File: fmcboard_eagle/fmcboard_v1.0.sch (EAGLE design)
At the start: 63 parts, among them IC1 OPA699ID, IC2 OPA699ID, IC3 ICL7660CPA, IC4 ICL7660CPA, IC5 LM358, J1 8pin, J12 4p-2.54, J2 ASP-134604-01, J3 4p-2.54, J4 4p-2.54, J5 8pin, J6 4p-2.54, Q1 BSS138, Q2 BSS138, Q3 BSS138, Q4 BSS138

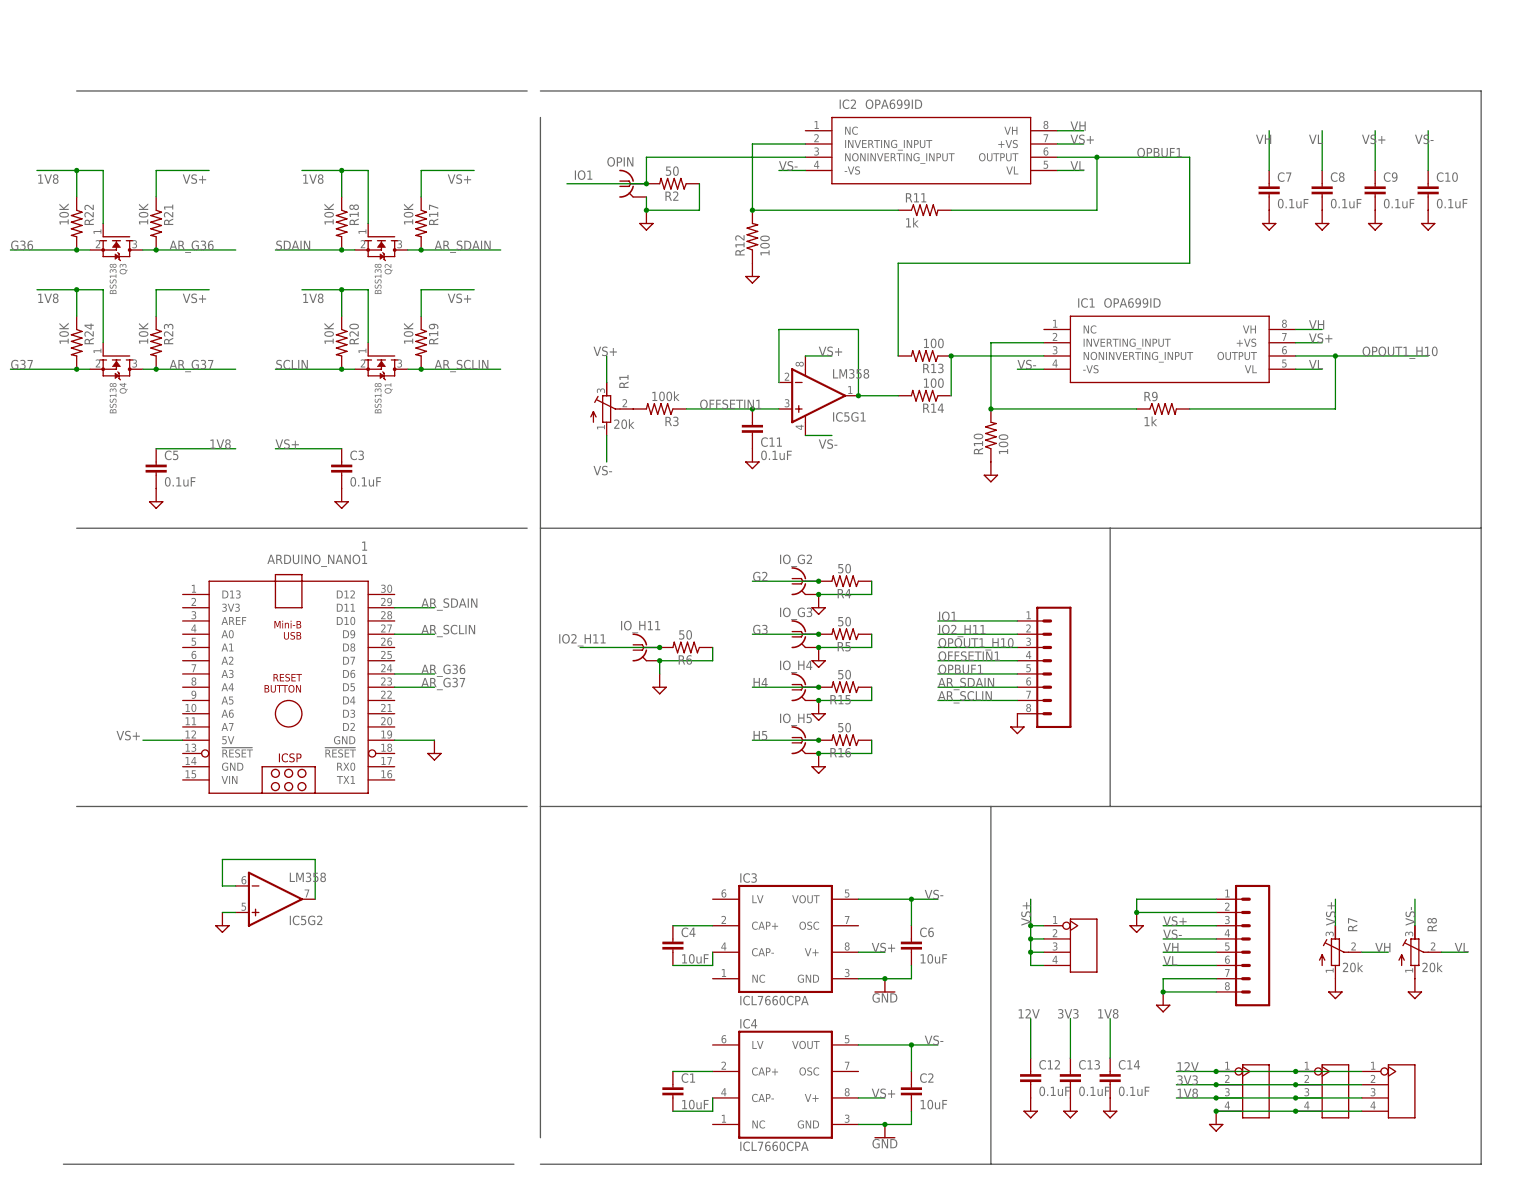
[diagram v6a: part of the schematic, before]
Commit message: Revert "use bss138 level shifting"
This reverts commit dd6467e355429a32c42db6855984b6cad7435a14.
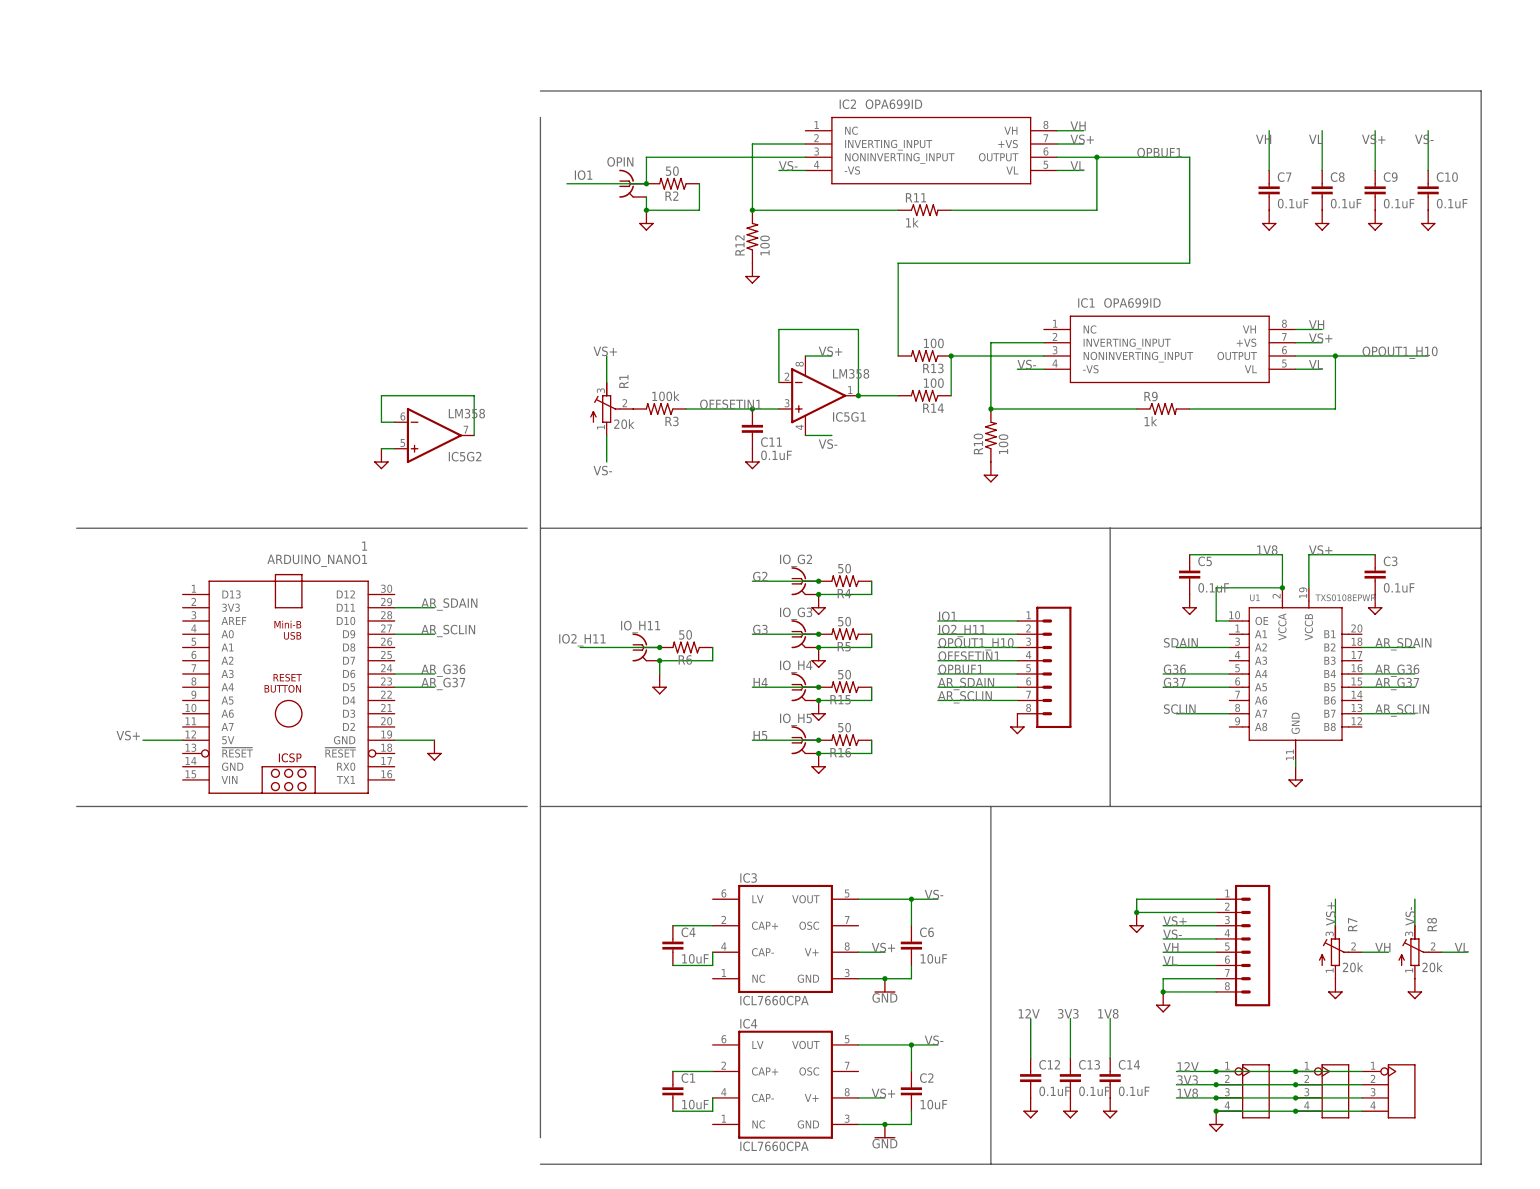
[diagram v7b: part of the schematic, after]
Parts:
- removed J6: 4p-2.54, Seeed-Connector:DIP-BLACK-FEMALE-HEADER-VERT(4P-2.54)
- removed Q1, Q2, Q3, Q4: BSS138, adafruit:MOSFET-NREFLOW
- removed R17, R18, R19, R20, R21, R22, R23, R24: 10K, adafruit:R-US_R0805
- added U1: TXS0108EPWR, Seeed-IC:LOGIC-TXS0108EPWR(TSSOP20)
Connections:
- net 1V8: now also U1.OE, U1.VCCA; no longer Q1.G, Q2.G, Q3.G, Q4.G, R18.1, R20.1, R22.1, R24.1
- net AR_G36: now also U1.B4; no longer Q3.D, R21.2
- net AR_G37: now also U1.B5; no longer Q4.D, R23.2
- net AR_SCLIN: now also U1.B7; no longer Q1.D, R19.2
- net AR_SDAIN: now also U1.B2; no longer Q2.D, R17.2
- net G36: now also U1.A4; no longer Q3.S, R22.2
- net G37: now also U1.A5; no longer Q4.S, R24.2
- net GND: now also U1.GND
- net SCLIN: now also U1.A7; no longer Q1.S, R20.2
- net SDAIN: now also U1.A2; no longer Q2.S, R18.2
- net VS+: now also U1.VCCB; no longer J6.P$1, J6.P$2, J6.P$3, J6.P$4, R17.1, R19.1, R21.1, R23.1
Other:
- note added: "Level shifter"
- note removed: "Level shifters (bss138 based)"
- moved on the sheet: C3, C5, IC5G2
